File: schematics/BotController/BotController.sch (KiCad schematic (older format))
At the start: 29 parts, among them IC1 ATMEGA644-P, P1 UM2102 - UART2USB, P10 Stepper Upperarm, P11 Stepper Shoulder, P2 Herkulex Servo, P3 Encoder Socket 0, P4 Encoder Socket, P5 Stepper 1 WristTurn, P6 POWER uC, P7 POWER_SERVO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

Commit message: no message
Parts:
- removed D4: LED grün, symbol LED
- removed IC1: ATMEGA644-P, DIL40, symbol ATMEGA644-P
- added D3: DIODE, Diodes_ThroughHole:Diode_DO-41_SOD81_Horizontal_RM10, symbol DIODE
- added IC1: ATMEGA644A-P, DIL40, symbol ATMEGA644A-P
- AVR1: footprint AVR-ISP-6 -> Pin_Headers:Pin_Header_Straight_2x03
- C1, C15, C16, C2: footprint (none) -> Capacitors_ThroughHole:C_Disc_D3_P2.5
- D1: footprint (none) -> Diodes_ThroughHole:Diode_DO-41_SOD81_Horizontal_RM10
- D2: footprint (none) -> LEDs:LED-3MM; symbol LED -> LED-RESCUE-BotController
- P1, P10, P11, P2, P3, P4, P5, P8, P9: footprint (none) -> Pin_Headers:Pin_Header_Straight_1x04
- P6, P7: footprint (none) -> Connect:bornier2
- R1, R2, R3, R4, R7: footprint (none) -> Discret:R4
- RV1: footprint (none) -> Potentiometers:Potentiometer_Trimmer-Piher_PT15-V12-5_horizontal
- SW2: footprint (none) -> Buttons_Switches_ThroughHole:SW_PUSH-12mm
- U1: footprint (none) -> Power_Integrations:TO-220
- X1: footprint (none) -> Oscillators:OSC_DIP8
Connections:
- wire segments 149 -> 145
- no-connect marks 8 -> 7
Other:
- moved on the sheet: R2

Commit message: no message
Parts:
- AVR1: footprint Pin_Headers:Pin_Header_Straight_2x03 -> BotController:AVR-ISP-6
- IC1: footprint DIL40 -> (none)
- X1: footprint Oscillators:OSC_DIP8 -> BotController:OSC_DIP14
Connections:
- net CLK2: now also IC1.34 ((PCINT6/ADC6)PA6); no longer IC1.33 ((PCINT7/ADC7)PA7)
- net DIR2: now also IC1.35 ((PCINT5/ADC5)PA5); no longer IC1.28 ((PCINT22/TOSC1)PC6), IC1.34 ((PCINT6/ADC6)PA6), P9.2 (P2)
- net EN2: now also IC1.36 ((PCINT4/ADC4)PA4); no longer IC1.35 ((PCINT5/ADC5)PA5)
- net EN3: now also IC1.33 ((PCINT7/ADC7)PA7); no longer IC1.26 ((PCINT20/TDO)PC4)
- net EN4: now also IC1.26 ((PCINT20/TDO)PC4); no longer IC1.21 ((PCINT31/OC2A)PD7)
- net En5: now also IC1.21 ((PCINT31/OC2A)PD7); no longer IC1.18 ((PCINT28/XCK1/OC1B)PD4)
- net RST: no longer IC1.29 ((PCINT23/TOSC2)PC7)
- net SCK: no longer IC1.23 ((PCINT17/SDA)PC1), P3.3 (P3), P4.3 (P3), R4.2
- net TAL: now reaches IC1.13 (XTAL1), X1.8 (TAL)
- new net DIR3: IC1.28 ((PCINT22/TOSC1)PC6), P9.2 (P2)
- new net SDA: IC1.23 ((PCINT17/SDA)PC1), P3.3 (P3), P4.3 (P3), R4.2
- no-connect marks 7 -> 6
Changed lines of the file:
@@
 	1    0    0    -1
 $EndComp
-Text Label 7600 4150 0    30   ~ 0
+Text Label 7600 4450 0    30   ~ 0
 MISO
 $Comp
@@
 F 0 "X1" H 3750 3300 60  0000 C CNN
 F 1 "CRYSTAL_OSSCI" H 3450 3000 60  0000 C CNN
-F 2 "Oscillators:OSC_DIP8" H 3450 3100 60  0001 C CNN
+F 2 "BotController:OSC_DIP14" H 3450 3100 60  0001 C CNN
 F 3 "" H 3450 3100 60  0001 C CNN
 	1    3450 3100
@@
 NoConn ~ 6050 3600
 NoConn ~ 6050 3500
-Text Label 7600 4800 0    30   ~ 0
+Text Label 7600 4650 0    30   ~ 0
 RST
-Text Label 7500 4200 0    30   ~ 0
+Text Label 7600 4550 0    30   ~ 0
 SCK
 NoConn ~ 30200 -14200
 NoConn ~ 4050 2700
-Text Label 8150 4450 0    30   ~ 0
+Text Label 7850 4550 0    30   ~ 0
 MOSI
 $Comp
@@
 F 0 "AVR1" H 7695 4740 50  0000 C CNN
 F 1 "AVR-ISP-6" H 7535 4270 50  0000 L BNN
-F 2 "Pin_Headers:Pin_Header_Straight_2x03" V 7255 4540 50  0001 C CNN
+F 2 "BotController:AVR-ISP-6" V 7255 4540 50  0001 C CNN
 F 3 "" H 7750 4550 60  0001 C CNN
 	1    7750 4550
@@
 Text Label 10800 3450 0    39   ~ 0
 EN3
-Text Label 10800 3550 0    39   ~ 0
-DIR2
 Text Label 10800 3650 0    39   ~ 0
 CLK3
@@
 Connection ~ 7850 1700
 Wire Wire Line
-	8150 6200 8150 4650
+	8150 4650 8150 6200
 Wire Wire Line
 	3850 2200 3850 2300
@@
 Connection ~ 11300 6200
 Wire Wire Line
-	10050 4800 6050 4800
-Wire Wire Line
-	10300 3100 10200 3100
-Wire Wire Line
-	10200 3100 10200 2900
-Wire Wire Line
-	10200 2900 6050 2900
+	10200 3100 10300 3100
+Wire Wire Line
+	10200 2800 10200 3100
 Wire Wire Line
 	6050 3200 7300 3200
@@
 	8500 3400 8400 3400
 Wire Wire Line
-	9600 3000 10300 3000
-Wire Wire Line
-	10300 3200 9500 3200
-Wire Wire Line
-	9500 3200 9500 3000
-Wire Wire Line
-	9500 3000 6050 3000
-Wire Wire Line
-	10800 3450 10500 3450
-Wire Wire Line
-	10500 3450 10500 4450
-Wire Wire Line
-	7000 4300 7000 4500
-Wire Wire Line
-	7000 4500 6050 4500
+	9600 3450 10800 3450
 Wire Wire Line
 	6050 4700 10600 4700
@@
 	6300 4600 6050 4600
 Wire Wire Line
-	11300 3900 11200 3900
-Wire Wire Line
-	11200 3900 11200 5700
-Wire Wire Line
-	11200 5700 6050 5700
+	10500 3900 11300 3900
+Wire Wire Line
+	11400 5700 6050 5700
 Wire Wire Line
 	6050 4400 6400 4400
@@
 	11750 4500 11400 4500
 Wire Wire Line
-	11400 4500 11400 5400
-Wire Wire Line
-	11400 5400 6050 5400
+	11400 4500 11400 5700
 Wire Wire Line
 	6050 5600 11500 5600
@@
 Wire Wire Line
 	11600 5500 6050 5500
-NoConn ~ 6050 2800
 Wire Wire Line
 	4850 6000 4850 6200
@@
 	1    0    0    -1
 $EndComp
-Wire Wire Line
-	10500 4450 8400 4450
-Wire Wire Line
-	8400 4450 8400 4300
-Wire Wire Line
-	8400 4300 7000 4300
 $Comp
 L DIODE D3
@@
 F 0 "IC1" H 4200 5880 50  0000 L BNN
 F 1 "ATMEGA644A-P" H 5450 2050 50  0000 L BNN
-F 2 "DIL40" H 5050 4000 50  0000 C CIN
+F 2 "" H 5050 4000 50  0001 C CIN
 F 3 "" H 5050 4000 50  0000 C CNN
 	1    5050 4000
@@
 Connection ~ 5050 1700
 Wire Wire Line
-	6050 2800 9600 2800
-Wire Wire Line
-	9600 2800 9600 3000
-Wire Wire Line
 	6050 3400 6250 3400
 Wire Wire Line
@@
 	8400 3400 8400 4100
 Connection ~ 8400 4100
+Wire Wire Line
+	9700 2700 9700 3000
+Wire Wire Line
+	9700 3000 10300 3000
+Wire Wire Line
+	9800 3200 10300 3200
+Wire Wire Line
+	9700 2700 6050 2700
+Wire Wire Line
+	6050 2900 9800 2900
+Wire Wire Line
+	6050 2800 10200 2800
+Wire Wire Line
+	9800 2900 9800 3200
+Wire Wire Line
+	6050 3000 9600 3000
+Wire Wire Line
+	9600 3000 9600 3450
+Wire Wire Line
+	10500 3900 10500 4250
+Wire Wire Line
+	10500 4250 6750 4250
+Wire Wire Line
+	6750 4250 6750 4500
+Wire Wire Line
+	6750 4500 6050 4500
+Text Label 10800 3550 0    39   ~ 0
+DIR3
+Text Label 11300 4200 0    39   ~ 0
+GND
+Text Label 11750 4800 0    39   ~ 0
+GND
+Text Label 4050 3100 0    39   ~ 0
+TAL
 $EndSCHEMATC

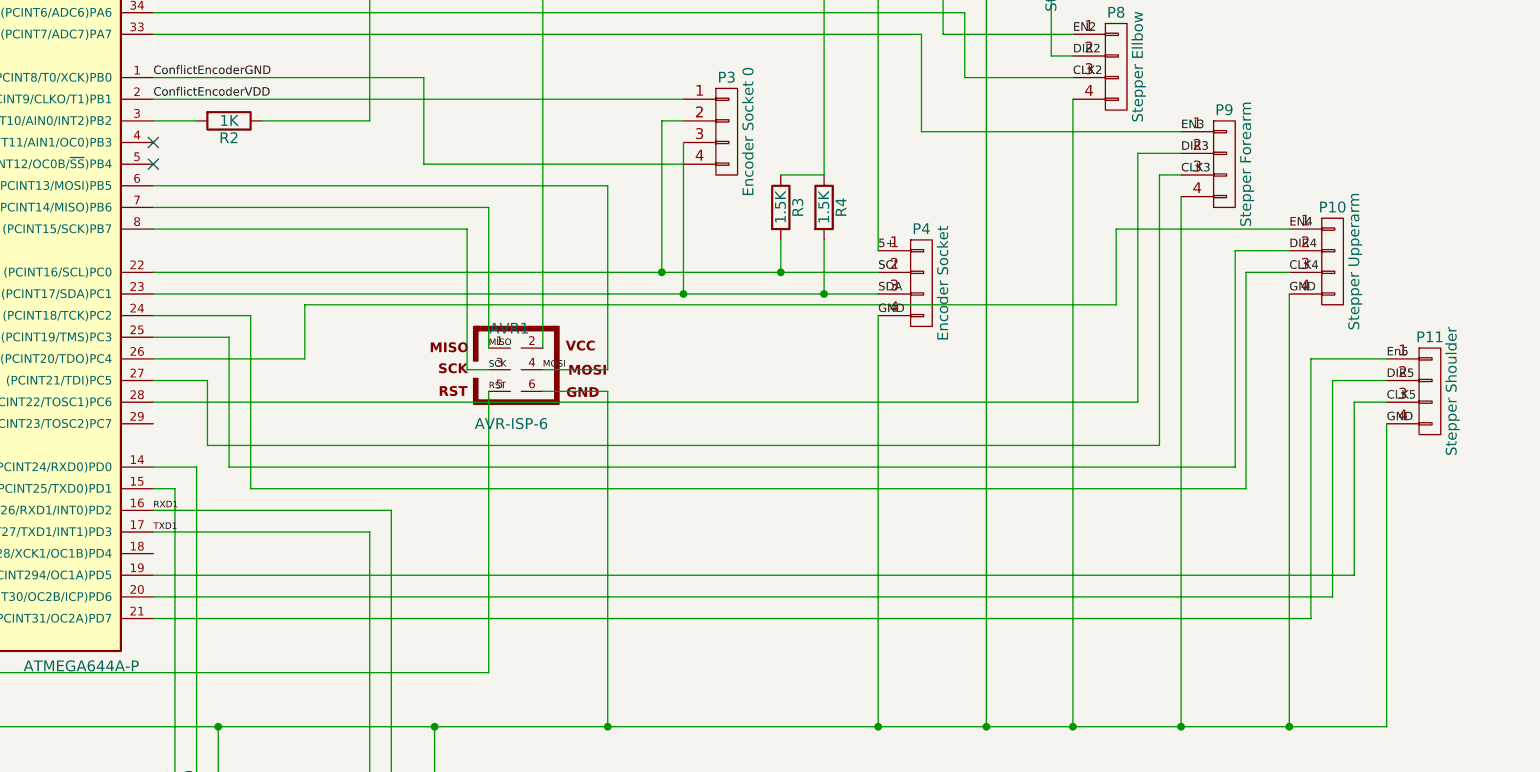
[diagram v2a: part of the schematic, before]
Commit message: beide Servos angesteuert und Handflansch korrigiert
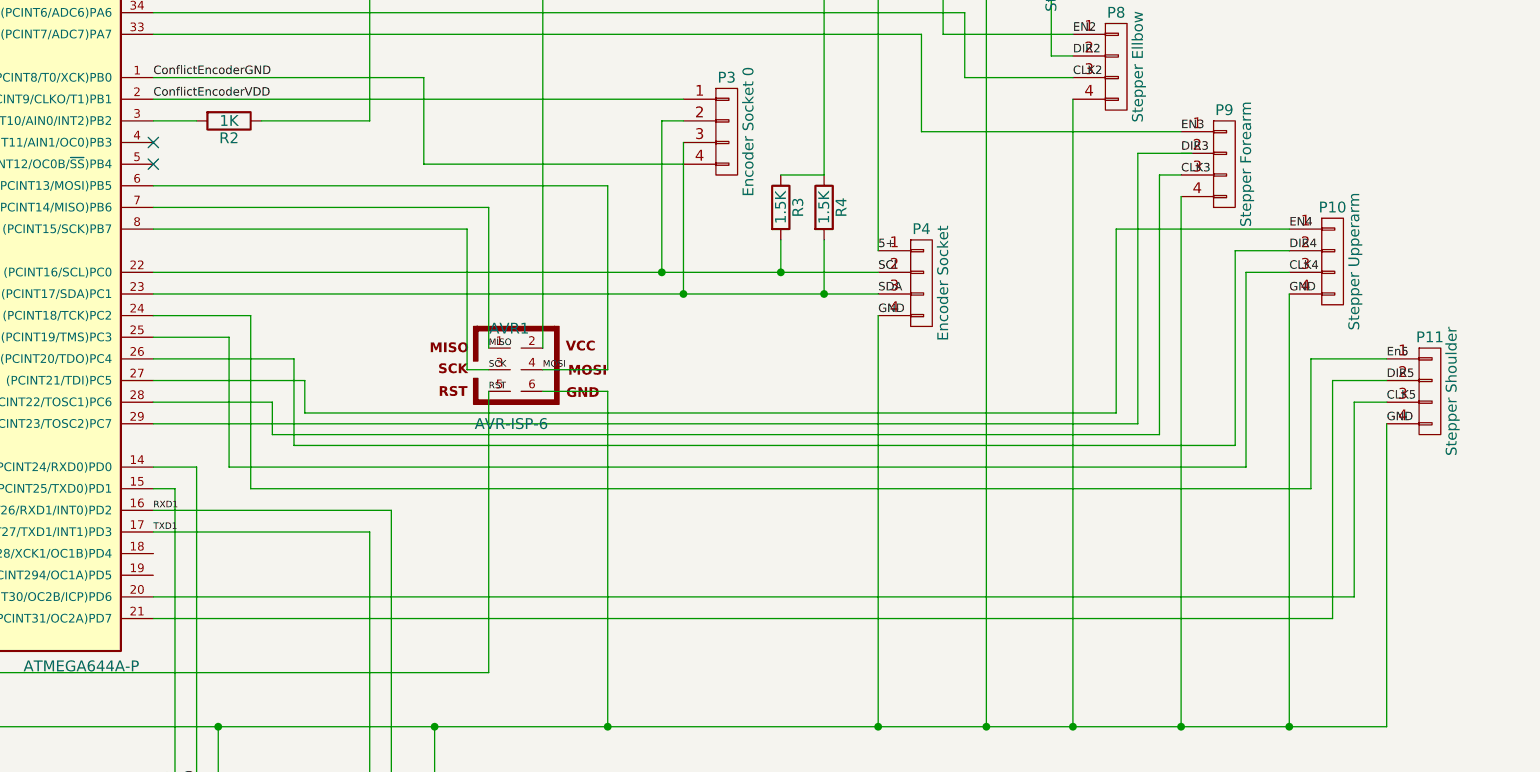
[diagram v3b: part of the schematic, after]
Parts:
- C1: footprint Capacitors_ThroughHole:C_Disc_D3_P2.5 -> Capacitors_ThroughHole:C_Radial_D8_L13_P3.8
- IC1: footprint (none) -> Housings_DIP:DIP-40_W15.24mm
- R4: footprint Discret:R4 -> Discret:R5
- U1: footprint Power_Integrations:TO-220 -> BotController:78XX-TO-220
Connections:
- net CLK3: now also IC1.28 ((PCINT22/TOSC1)PC6); no longer IC1.27 ((PCINT21/TDI)PC5)
- net CLK4: now also IC1.25 ((PCINT19/TMS)PC3); no longer IC1.24 ((PCINT18/TCK)PC2)
- net CLK5: now also IC1.20 ((PCINT30/OC2B/ICP)PD6); no longer IC1.19 ((PCINT294/OC1A)PD5)
- net DIR3: now also IC1.29 ((PCINT23/TOSC2)PC7); no longer IC1.28 ((PCINT22/TOSC1)PC6)
- net DIR4: now also IC1.26 ((PCINT20/TDO)PC4); no longer IC1.25 ((PCINT19/TMS)PC3)
- net DIR5: now also IC1.21 ((PCINT31/OC2A)PD7); no longer IC1.20 ((PCINT30/OC2B/ICP)PD6)
- net EN4: now also IC1.27 ((PCINT21/TDI)PC5); no longer IC1.26 ((PCINT20/TDO)PC4)
- net En5: now also IC1.24 ((PCINT18/TCK)PC2); no longer IC1.21 ((PCINT31/OC2A)PD7)
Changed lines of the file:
@@
 EESchema Schematic File Version 2
 LIBS:BotController-rescue
-LIBS:power
-LIBS:device
-LIBS:transistors
-LIBS:conn
-LIBS:linear
-LIBS:regul
-LIBS:74xx
-LIBS:cmos4000
-LIBS:adc-dac
-LIBS:memory
-LIBS:xilinx
-LIBS:microcontrollers
-LIBS:dsp
-LIBS:microchip
-LIBS:analog_switches
-LIBS:motorola
-LIBS:texas
-LIBS:intel
-LIBS:audio
-LIBS:interface
-LIBS:digital-audio
-LIBS:philips
-LIBS:display
-LIBS:cypress
-LIBS:siliconi
-LIBS:opto
-LIBS:atmel
-LIBS:contrib
-LIBS:valves
 LIBS:BotController-cache
 EELAYER 25 0
@@
 F 0 "R4" V 9230 3800 50  0000 C CNN
 F 1 "1.5K" V 9150 3800 50  0000 C CNN
-F 2 "Discret:R4" V 9080 3800 30  0001 C CNN
+F 2 "Discret:R5" V 9080 3800 30  0001 C CNN
 F 3 "" H 9150 3800 30  0000 C CNN
 	1    9150 3800
@@
 F 0 "U1" H 2800 7004 60  0000 C CNN
 F 1 "7805" H 2650 7400 60  0000 C CNN
-F 2 "Power_Integrations:TO-220" H 2650 7200 60  0001 C CNN
+F 2 "BotController:78XX-TO-220" H 2650 7200 60  0001 C CNN
 F 3 "" H 2650 7200 60  0000 C CNN
 	1    2650 7200
@@
 F 0 "C1" H 2075 7600 50  0000 L CNN
 F 1 "100uF" H 2075 7400 50  0000 L CNN
-F 2 "Capacitors_ThroughHole:C_Disc_D3_P2.5" H 2088 7350 30  0001 C CNN
+F 2 "Capacitors_ThroughHole:C_Radial_D8_L13_P3.8" H 2088 7350 30  0001 C CNN
 F 3 "" H 2050 7500 60  0000 C CNN
 	1    2050 7500
@@
 	9600 3450 10800 3450
 Wire Wire Line
-	6050 4700 10600 4700
-Wire Wire Line
-	10600 4700 10600 3550
-Wire Wire Line
-	10600 3550 10800 3550
-Wire Wire Line
 	10800 3650 10700 3650
 Wire Wire Line
-	10700 3650 10700 4900
-Wire Wire Line
-	10700 4900 6300 4900
-Wire Wire Line
-	6300 4900 6300 4600
-Wire Wire Line
-	6300 4600 6050 4600
-Wire Wire Line
 	10500 3900 11300 3900
 Wire Wire Line
-	11400 5700 6050 5700
-Wire Wire Line
 	6050 4400 6400 4400
 Wire Wire Line
 	6400 4400 6400 5000
 Wire Wire Line
-	6400 5000 11050 5000
-Wire Wire Line
-	11050 5000 11050 4000
-Wire Wire Line
 	11050 4000 11300 4000
 Wire Wire Line
 	11300 4100 11100 4100
 Wire Wire Line
-	11100 4100 11100 5100
-Wire Wire Line
-	11100 5100 6500 5100
-Wire Wire Line
 	6500 5100 6500 4300
 Wire Wire Line
 	6500 4300 6050 4300
 Wire Wire Line
-	11750 4500 11400 4500
-Wire Wire Line
-	11400 4500 11400 5700
-Wire Wire Line
-	6050 5600 11500 5600
-Wire Wire Line
-	11500 5600 11500 4600
-Wire Wire Line
 	11500 4600 11750 4600
 Wire Wire Line
 	11750 4700 11600 4700
 Wire Wire Line
-	11600 4700 11600 5500
-Wire Wire Line
-	11600 5500 6050 5500
+	11600 4700 11600 5600
 Wire Wire Line
 	4850 6000 4850 6200
@@
 F 0 "IC1" H 4200 5880 50  0000 L BNN
 F 1 "ATMEGA644A-P" H 5450 2050 50  0000 L BNN
-F 2 "" H 5050 4000 50  0001 C CIN
+F 2 "Housings_DIP:DIP-40_W15.24mm" H 5050 4000 50  0001 C CIN
 F 3 "" H 5050 4000 50  0000 C CNN
 	1    5050 4000
@@
 	9600 3000 9600 3450
 Wire Wire Line
-	10500 3900 10500 4250
-Wire Wire Line
-	10500 4250 6750 4250
-Wire Wire Line
-	6750 4250 6750 4500
-Wire Wire Line
-	6750 4500 6050 4500
+	10500 3900 10500 4750
 Text Label 10800 3550 0    39   ~ 0
 DIR3
@@
 Text Label 4050 3100 0    39   ~ 0
 TAL
+Wire Wire Line
+	10850 3550 10600 3550
+Wire Wire Line
+	10600 3550 10600 4800
+Wire Wire Line
+	10600 4800 6050 4800
+Wire Wire Line
+	10700 3650 10700 4850
+Wire Wire Line
+	10700 4850 6600 4850
+Wire Wire Line
+	6600 4850 6600 4700
+Wire Wire Line
+	6600 4700 6050 4700
+Wire Wire Line
+	10500 4750 6750 4750
+Wire Wire Line
+	6750 4750 6750 4600
+Wire Wire Line
+	6750 4600 6050 4600
+Wire Wire Line
+	11050 4000 11050 4900
+Wire Wire Line
+	11050 4900 6700 4900
+Wire Wire Line
+	6700 4900 6700 4500
+Wire Wire Line
+	6700 4500 6050 4500
+Wire Wire Line
+	11100 4100 11100 5000
+Wire Wire Line
+	11100 5000 6400 5000
+Wire Wire Line
+	6500 5100 11400 5100
+Wire Wire Line
+	11400 5100 11400 4500
+Wire Wire Line
+	11400 4500 11750 4500
+Wire Wire Line
+	11500 4600 11500 5700
+Wire Wire Line
+	11500 5700 6050 5700
+Wire Wire Line
+	11600 5600 6050 5600
 $EndSCHEMATC
